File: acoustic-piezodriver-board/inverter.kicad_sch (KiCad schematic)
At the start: 40 parts, among them P201 WJ128V-5.0-3P, U201 UCC27282DR, U202 UCC27282DR, U204 TMCS1108A3UQDR, U6 NCE6005AS, U7 NCE6005AS

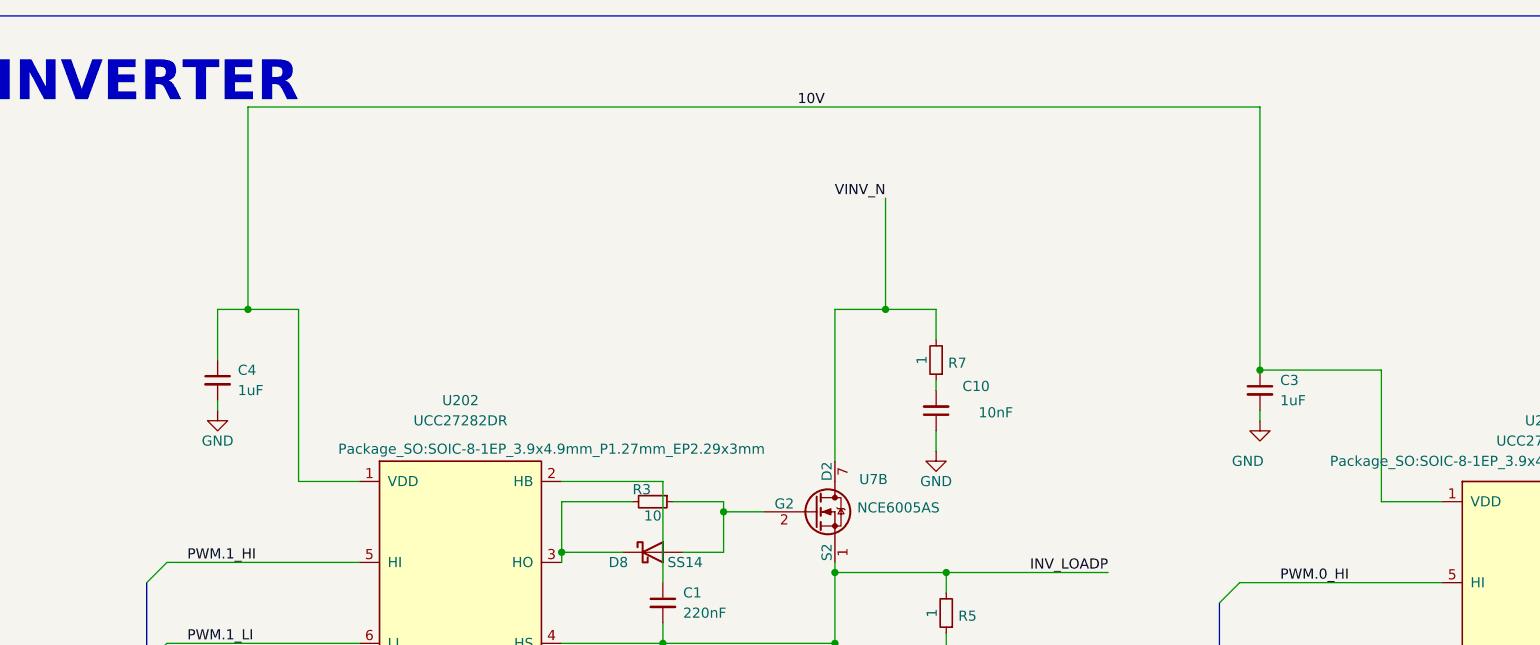
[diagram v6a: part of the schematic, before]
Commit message: main routing completed, finish 3V3 + I2C bus
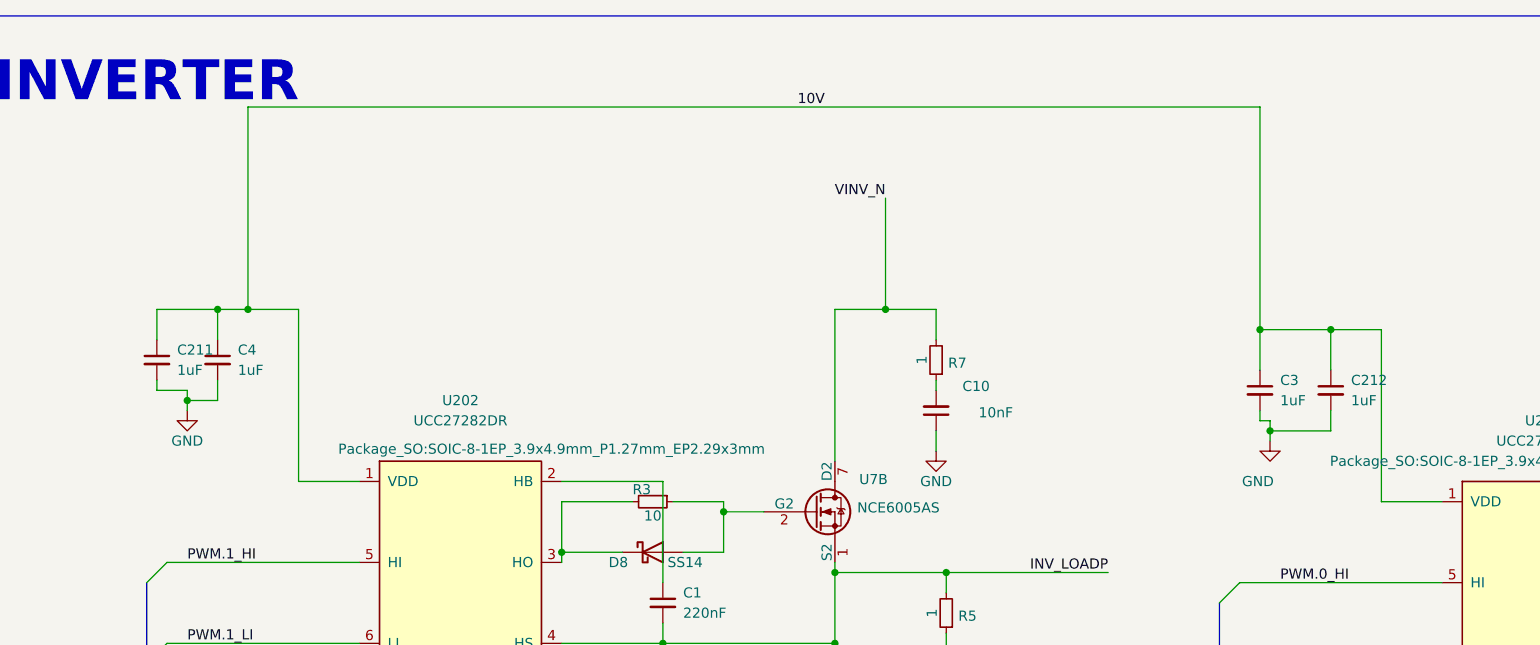
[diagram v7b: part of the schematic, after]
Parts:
- added C211, C212: 1uF, Capacitor_SMD:C_0805_2012Metric, symbol Device:C_Small
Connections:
- net 10V: now also C211.1, C212.1
- net GND: now also C211.2, C212.2
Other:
- moved on the sheet: C4

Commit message: Fixed ERC, DRC errors, finished routing (next) perform footprint checks
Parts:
- R10, R5, R6, R7, R8, R9: footprint Capacitor_SMD:C_0603_1608Metric -> Resistor_SMD:R_0603_1608Metric
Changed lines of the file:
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@@
 			)
 		)
-		(property "Footprint" "Capacitor_SMD:C_0603_1608Metric"
+		(property "Footprint" "Resistor_SMD:R_0603_1608Metric"
 			(at 135.89 93.98 0)
 			(effects
@@
 			)
 		)
-		(property "Footprint" "Capacitor_SMD:C_0603_1608Metric"
+		(property "Footprint" "Resistor_SMD:R_0603_1608Metric"
 			(at 134.62 62.23 0)
 			(effects
@@
 			)
 		)
-		(property "Footprint" "Capacitor_SMD:C_0603_1608Metric"
+		(property "Footprint" "Resistor_SMD:R_0603_1608Metric"
 			(at 265.43 100.33 0)
 			(effects
@@
 			)
 		)
-		(property "Footprint" "Capacitor_SMD:C_0603_1608Metric"
+		(property "Footprint" "Resistor_SMD:R_0603_1608Metric"
 			(at 264.16 124.46 0)
 			(effects
@@
 			)
 		)
-		(property "Footprint" "Capacitor_SMD:C_0603_1608Metric"
+		(property "Footprint" "Resistor_SMD:R_0603_1608Metric"
 			(at 265.43 74.93 0)
 			(effects
@@
 			)
 		)
-		(property "Datasheet" "~"
+		(property "Datasheet" "https://jlcpcb.com/api/file/downloadByFileSystemAccessId/8590903989825183744"
 			(at 349.25 176.53 0)
 			(effects
@@
 			)
 		)
-		(property "Footprint" "Capacitor_SMD:C_0603_1608Metric"
+		(property "Footprint" "Resistor_SMD:R_0603_1608Metric"
 			(at 129.54 128.27 0)
 			(effects
@@
 			)
 		)
-		(property "Datasheet" "~"
+		(property "Datasheet" "https://jlcpcb.com/api/file/downloadByFileSystemAccessId/8590903989825183744"
 			(at 334.01 176.53 0)
 			(effects
@@
 			)
 		)
-		(property "Datasheet" "~"
+		(property "Datasheet" "https://jlcpcb.com/api/file/downloadByFileSystemAccessId/8590903989825183744"
 			(at 317.5 176.53 0)
 			(effects
